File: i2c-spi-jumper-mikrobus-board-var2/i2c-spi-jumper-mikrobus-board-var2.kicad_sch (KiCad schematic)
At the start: 10 parts, among them J1 mikroBUS_L, J2 mikroBUS_R, U1 SC18IS606PW

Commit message: i2c-spi-jumper-var2: fix LCSC number of chip
we had the old one listed
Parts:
- U1: LCSC C2678036 -> C5190384
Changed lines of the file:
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@@
       (effects (font (size 1.27 1.27)) hide)
     )
-    (property "LCSC" "C2678036" (id 4) (at 140.97 85.725 0)
+    (property "LCSC" "C5190384" (id 4) (at 140.97 85.725 0)
       (effects (font (size 1.27 1.27)) hide)
     )

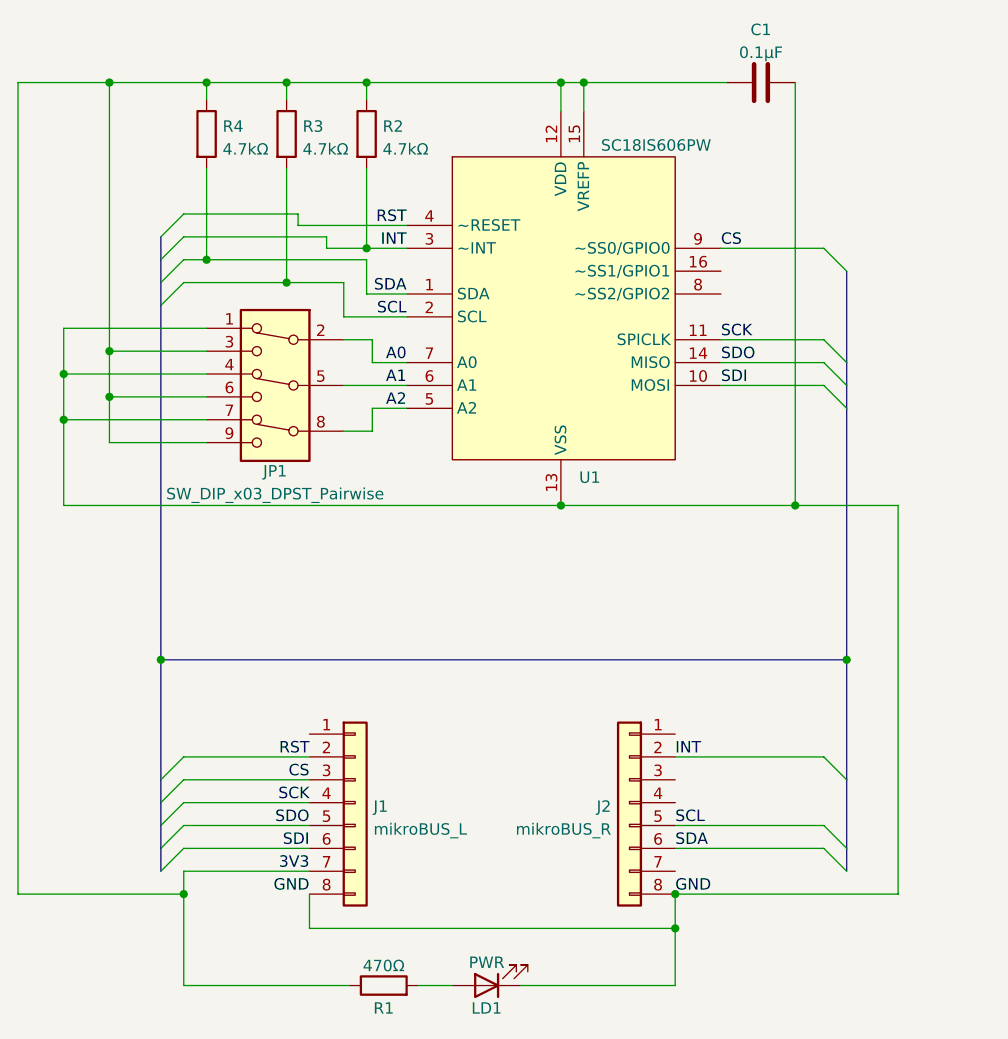
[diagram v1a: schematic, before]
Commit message: i2c-spi-jumper-var2: fix signal negation
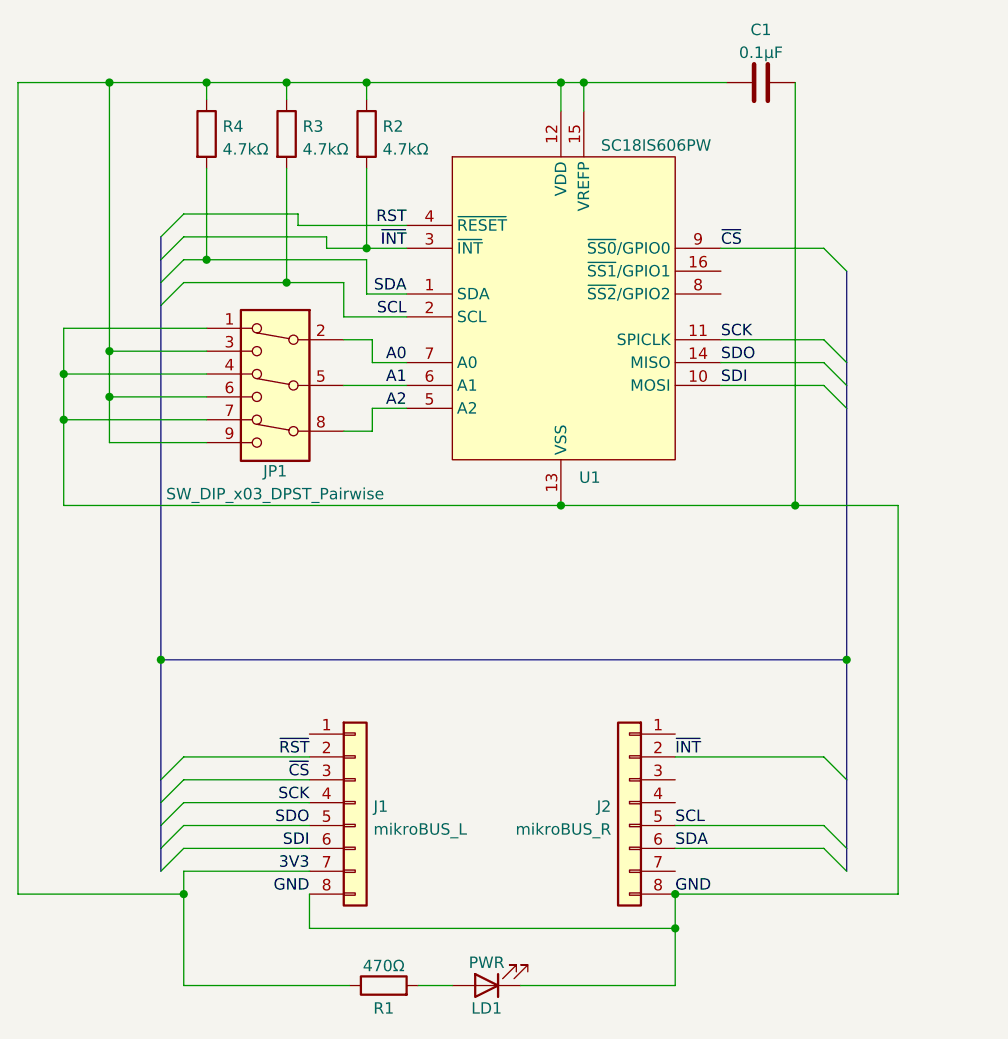
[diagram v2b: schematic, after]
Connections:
- net RST: no longer J1.2 (Pin_2)
- net CS renamed ~{CS}
- net INT renamed ~{INT}
- new net ~{RST}: J1.2 (Pin_2)
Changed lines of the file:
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@@
     (effects (font (size 1.27 1.27)) (justify right bottom))
   )
-  (label "RST" (at 113.03 135.89 180)
+  (label "~{RST}" (at 113.03 135.89 180)
     (effects (font (size 1.27 1.27)) (justify right bottom))
   )
@@
     (effects (font (size 1.27 1.27)) (justify right bottom))
   )
-  (label "CS" (at 113.03 138.43 180)
+  (label "~{CS}" (at 113.03 138.43 180)
     (effects (font (size 1.27 1.27)) (justify right bottom))
   )
@@
     (effects (font (size 1.27 1.27)) (justify right bottom))
   )
-  (label "INT" (at 153.67 135.89 0)
+  (label "~{INT}" (at 153.67 135.89 0)
     (effects (font (size 1.27 1.27)) (justify left bottom))
   )
-  (label "CS" (at 158.75 79.375 0)
+  (label "~{CS}" (at 158.75 79.375 0)
     (effects (font (size 1.27 1.27)) (justify left bottom))
   )
-  (label "INT" (at 123.825 79.375 180)
+  (label "~{INT}" (at 123.825 79.375 180)
     (effects (font (size 1.27 1.27)) (justify right bottom))
   )

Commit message: i2c-spi-jumper-var2: add jumper to enable/disable ~INT pin connection
This allows mikroBUS boards like the OLED C click to be used with this
board without causing their Enable pin, which shares its location with the
~Interrupt pin, to be pulled low after SPI communication completes.
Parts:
- added JP2: INT_Jumper, Connector_PinHeader_2.54mm:PinHeader_1x02_P2.54mm_Vertical, symbol Jumper:Jumper_2_Open
- J1, J2, JP1: now left out of the parts list
- LD1: footprint LED_SMD:LED_0805_2012Metric -> LED_SMD:LED_0603_1608Metric; LCSC C73548 -> C72043; Manufacturer Everlight -> (none); Model 17-21SYGC/S530-E2/TR8 -> (none); Package 0805 -> 0603
- R1: footprint Resistor_SMD:R_0805_2012Metric -> Resistor_SMD:R_0603_1608Metric; LCSC C17673 -> C23179; Package 0805 -> 0603
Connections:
- net RST is gone; now on net ~{RST}: U1.4 (~{RESET})
- net ~{INT}: now also JP2.2 (B); no longer J2.2 (Pin_2)
- new net: J2.2 (Pin_2), JP2.1 (A)
